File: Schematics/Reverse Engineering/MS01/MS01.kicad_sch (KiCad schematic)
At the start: 69 parts, among them Q1 S1007, Q10 PNP, Q11 PNP, Q12 PNP, Q2 2N1304, Q3 PNP, Q4 2N1304, Q5 2N1304, Q6 PNP, Q7 PNP, Q8 PNP, Q9 PNP, U1 RLIC-12D

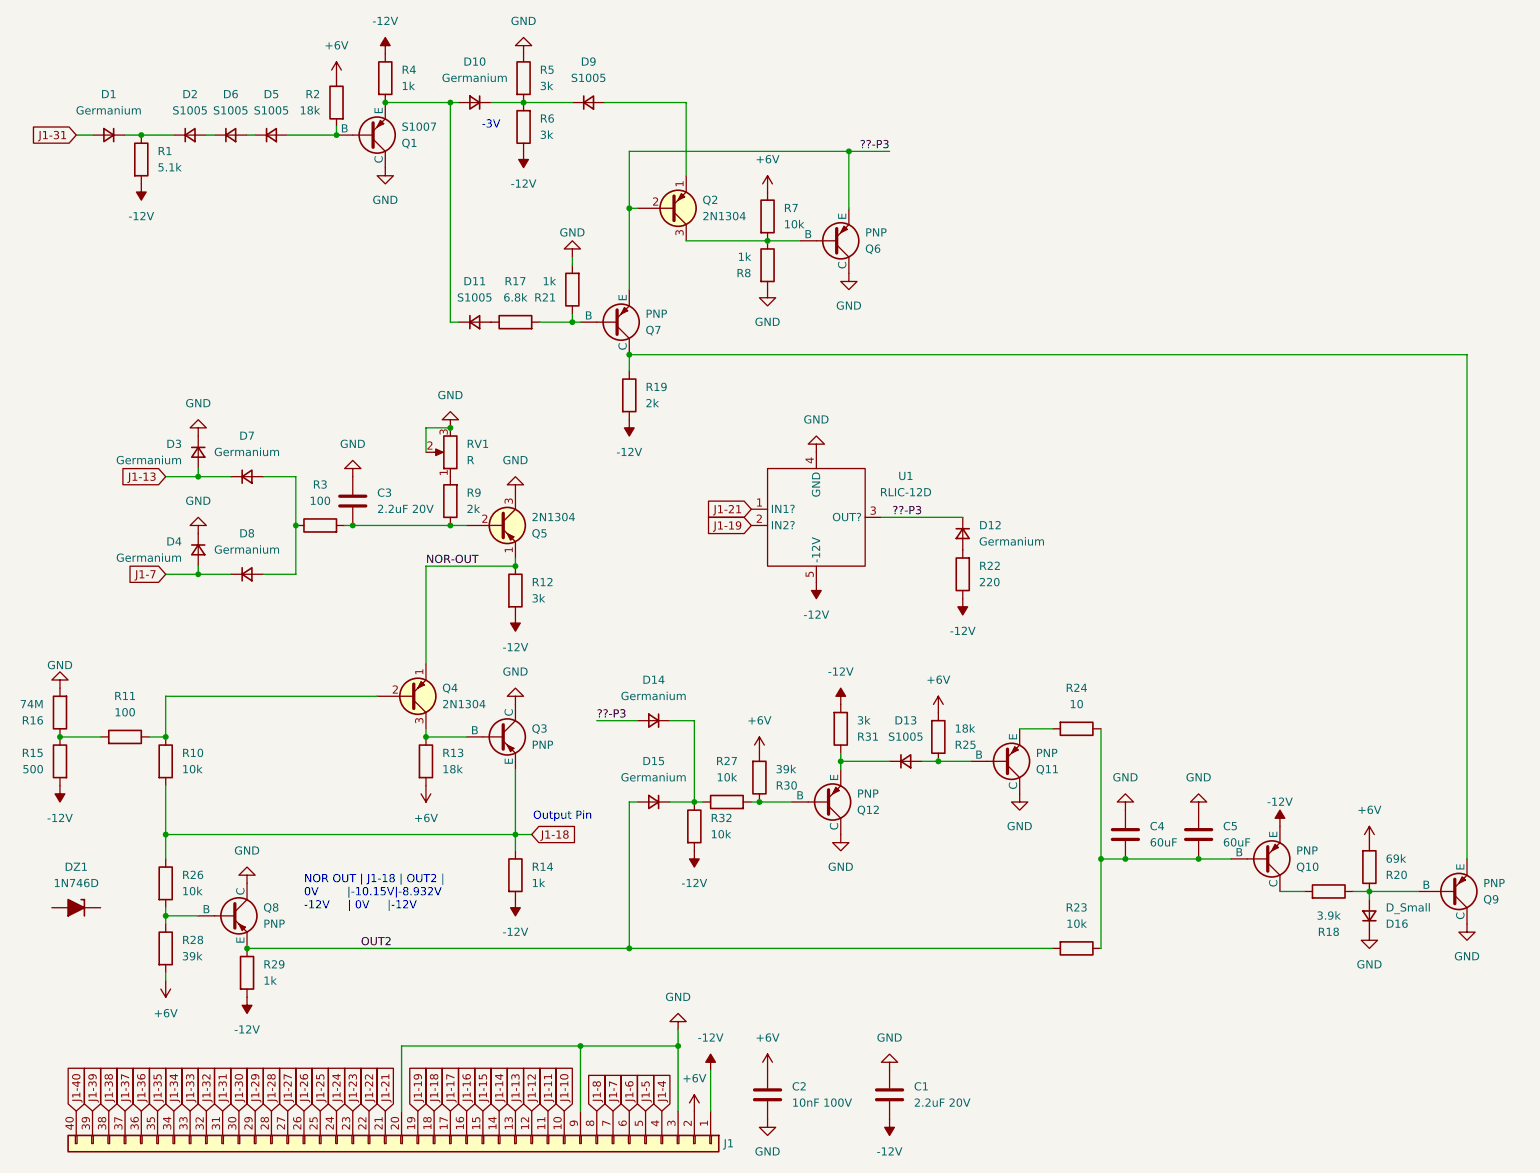
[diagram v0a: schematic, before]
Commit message: MS01 Reverse Engineering
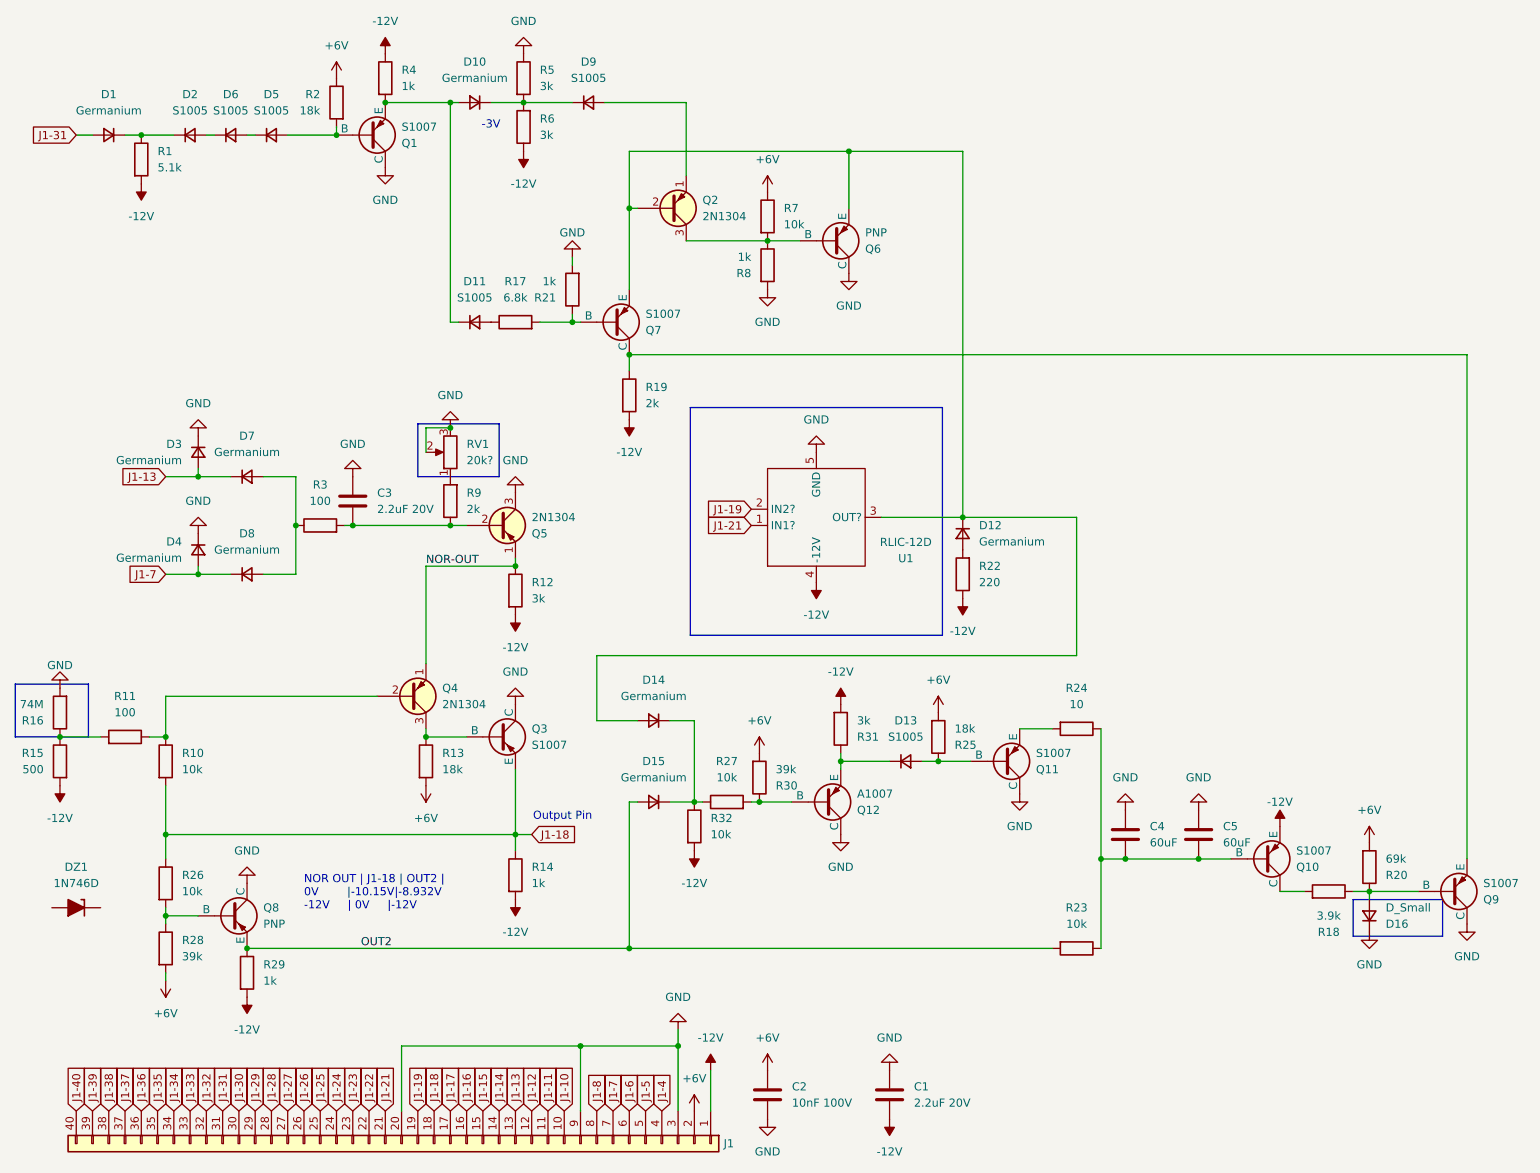
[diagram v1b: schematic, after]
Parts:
- Q10, Q11, Q3, Q7, Q9: value PNP -> S1007
- Q12: value PNP -> A1007
- RV1: value R -> 20k?
- U1: footprint (none) -> MS01:RLIC-12D
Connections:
- net -12V: now also U1.4 (-12V); no longer U1.5 (-12V)
- net GND: now also U1.5 (GND); no longer U1.4 (GND)
- net ??-P3: no longer names the net of D12.1 (K), D14.2 (A), Q2.2 (B), Q6.3 (E), Q7.3 (E), U1.3 (OUT?)
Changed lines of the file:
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@@
 	(generator_version "9.0")
 	(paper "A4")
+	(rectangle
+		(start 13.335 118.745)
+		(end 24.765 127)
+		(stroke
+			(width 0)
+			(type default)
+		)
+		(fill
+			(type none)
+		)
+	)
+	(rectangle
+		(start 76.2 78.105)
+		(end 88.9 86.36)
+		(stroke
+			(width 0)
+			(type default)
+		)
+		(fill
+			(type none)
+		)
+	)
+	(rectangle
+		(start 118.745 75.565)
+		(end 158.115 111.125)
+		(stroke
+			(width 0)
+			(type default)
+		)
+		(fill
+			(type none)
+		)
+	)
+	(rectangle
+		(start 222.25 152.4)
+		(end 236.22 158.115)
+		(stroke
+			(width 0)
+			(type default)
+		)
+		(fill
+			(type none)
+		)
+	)
 	(text "-3V"
 		(exclude_from_sim no)
@@
 	)
 	(junction
+		(at 161.29 92.71)
+		(diameter 0)
+		(color 0 0 0 0)
+	)
+	(junction
 		(at 116.84 175.26)
 		(diameter 0)
@@
 	(wire
 		(pts
+			(xy 104.14 114.3) (xy 179.07 114.3)
+		)
+		(stroke
+			(width 0)
+			(type default)
+		)
+	)
+	(wire
+		(pts
 			(xy 119.38 124.46) (xy 119.38 137.16)
 		)
@@
 	(wire
 		(pts
+			(xy 179.07 92.71) (xy 161.29 92.71)
+		)
+		(stroke
+			(width 0)
+			(type default)
+		)
+	)
+	(wire
+		(pts
 			(xy 41.91 85.09) (xy 41.91 86.36)
 		)
@@
 	(wire
 		(pts
-			(xy 149.86 35.56) (xy 143.51 35.56)
+			(xy 143.51 35.56) (xy 161.29 35.56)
 		)
 		(stroke
@@
 	(wire
 		(pts
+			(xy 161.29 92.71) (xy 161.29 35.56)
+		)
+		(stroke
+			(width 0)
+			(type default)
+		)
+	)
+	(wire
+		(pts
 			(xy 92.71 27.94) (xy 87.63 27.94)
 		)
@@
 	(wire
 		(pts
+			(xy 179.07 114.3) (xy 179.07 92.71)
+		)
+		(stroke
+			(width 0)
+			(type default)
+		)
+	)
+	(wire
+		(pts
 			(xy 77.47 100.33) (xy 77.47 115.57)
 		)
@@
 	(wire
 		(pts
+			(xy 104.14 124.46) (xy 104.14 114.3)
+		)
+		(stroke
+			(width 0)
+			(type default)
+		)
+	)
+	(wire
+		(pts
 			(xy 109.22 67.31) (xy 240.03 67.31)
 		)
@@
 		)
 	)
-	(label "??-P3"
-		(at 149.86 35.56 180)
-		(effects
-			(font
-				(size 1.27 1.27)
-			)
-			(justify right bottom)
-		)
-	)
-	(label "??-P3"
-		(at 154.94 92.71 180)
-		(effects
-			(font
-				(size 1.27 1.27)
-			)
-			(justify right bottom)
-		)
-	)
-	(label "??-P3"
-		(at 104.14 124.46 0)
-		(effects
-			(font
-				(size 1.27 1.27)
-			)
-			(justify left bottom)
-		)
-	)
 	(label "OUT2"
 		(at 67.31 160.02 0)
@@
 	(global_label "J1-19"
 		(shape input)
-		(at 128.27 93.98 180)
+		(at 128.27 91.44 180)
 		(fields_autoplaced yes)
 		(effects
@@
 		)
 		(property "Intersheetrefs" "${INTERSHEET_REFS}"
-			(at 119.1163 93.98 0)
+			(at 119.1163 91.44 0)
 			(effects
 				(font
@@
 	(global_label "J1-21"
 		(shape input)
-		(at 128.27 91.44 180)
+		(at 128.27 93.98 180)
 		(fields_autoplaced yes)
 		(effects
@@
 		)
 		(property "Intersheetrefs" "${INTERSHEET_REFS}"
-			(at 119.1163 91.44 0)
+			(at 119.1163 93.98 0)
 			(effects
 				(font
@@
 			)
 		)
-		(property "Value" "PNP"
+		(property "Value" "S1007"
 			(at 172.72 129.5401 0)
 			(effects
@@
 			)
 		)
-		(property "Value" "R"
+		(property "Value" "20k?"
 			(at 83.82 83.8199 0)
 			(effects
@@
 			)
 		)
-		(property "Value" "PNP"
+		(property "Value" "S1007"
 			(at 213.36 144.7801 0)
 			(effects
@@
 	(symbol
 		(lib_id "power:-12V")
-		(at 138.43 102.87 180)
+		(at 138.43 102.87 0)
+		(mirror x)
 		(unit 1)
 		(exclude_from_sim no)
@@
 			)
 		)
-		(property "Value" "PNP"
+		(property "Value" "S1007"
 			(at 242.57 149.8601 0)
 			(effects
@@
 			)
 		)
-		(property "Value" "PNP"
+		(property "Value" "S1007"
 			(at 111.76 60.9601 0)
 			(effects
@@
 		(lib_id "MS01:RLIC-12D")
 		(at 138.43 92.71 0)
+		(mirror x)
 		(unit 1)
 		(exclude_from_sim no)
@@
 		(fields_autoplaced yes)
 		(property "Reference" "U1"
-			(at 152.4 86.2898 0)
+			(at 152.4 99.1302 0)
 			(effects
 				(font
@@
 		)
 		(property "Value" "RLIC-12D"
-			(at 152.4 88.8298 0)
+			(at 152.4 96.5902 0)
 			(effects
 				(font
@@
 			)
 		)
-		(property "Footprint" ""
+		(property "Footprint" "MS01:RLIC-12D"
 			(at 138.43 92.71 0)
 			(effects
@@
 	(symbol
 		(lib_id "power:GND")
-		(at 138.43 82.55 180)
+		(at 138.43 82.55 0)
+		(mirror x)
 		(unit 1)
 		(exclude_from_sim no)
@@
 			)
 		)
-		(property "Value" "PNP"
+		(property "Value" "S1007"
 			(at 93.98 128.2699 0)
 			(effects
@@
 			)
 		)
-		(property "Value" "PNP"
+		(property "Value" "A1007"
 			(at 144.78 135.8901 0)
 			(effects

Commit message: Finished MS01 PCB and Revised Schematic
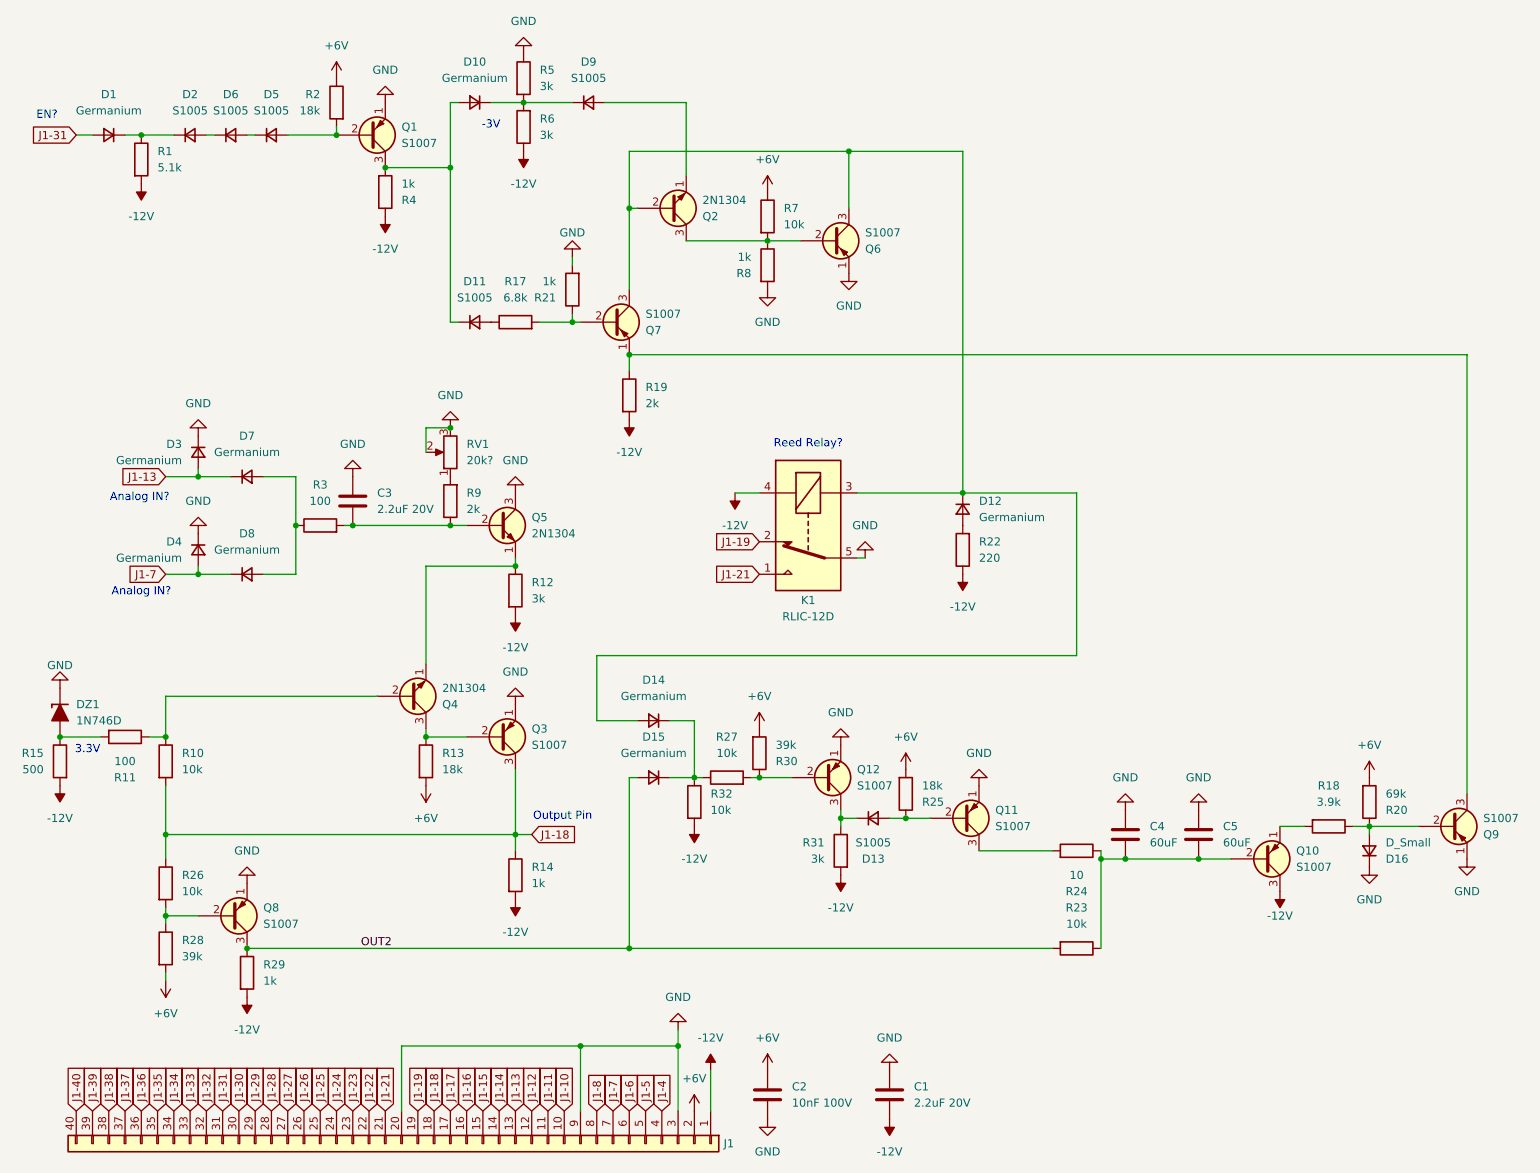
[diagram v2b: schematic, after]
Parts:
- removed Q1: S1007, Package_TO_SOT_THT:TO-5-3, symbol Simulation_SPICE:PNP
- removed Q2, Q4, Q5: 2N1304, Package_TO_SOT_THT:TO-5-3, symbol PCM_Transistor_BJT_AKL:Q_PNP_Generic_EBC
- removed R16: 74M, Resistor_THT:R_Axial_DIN0207_L6.3mm_D2.5mm_P10.16mm_Horizontal, symbol Device:R
- added Q1: S1007, Package_TO_SOT_THT:TO-5-3, symbol PCM_Transistor_BJT_AKL:Q_PNP_Generic_EBC
- added Q2, Q4, Q5: 2N1304, Package_TO_SOT_THT:TO-5-3, symbol PCM_Transistor_BJT_AKL:Q_NPN_Generic_EBC
- DZ1: footprint (none) -> Diode_THT:D_A-405_P12.70mm_Horizontal
- Q10, Q11, Q3, Q7, Q9: symbol Simulation_SPICE:PNP -> PCM_Transistor_BJT_AKL:Q_PNP_Generic_EBC
- Q12: value A1007 -> S1007; symbol Simulation_SPICE:PNP -> PCM_Transistor_BJT_AKL:Q_PNP_Generic_EBC
- Q6, Q8: value PNP -> S1007; symbol Simulation_SPICE:PNP -> PCM_Transistor_BJT_AKL:Q_PNP_Generic_EBC
- renumbered U1 to K1
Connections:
- net GND: now also DZ1.1 (K), Q1.1 (E), Q5.3 (C)
- net at D5.2 (A), R2.2: now also Q1.2 (B)
- net at D10.2 (A), D11.1 (K), R4.2: now also Q1.3 (C)
- net at R10.1, R11.1: now also Q4.2 (B)
- net at R11.2, R15.1: now also DZ1.2 (A)
- net at Q6.2 (B), R7.2, R8.1: now also Q2.3 (C)
- net at D12.1 (K), D14.2 (A), K1.3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: now also Q2.2 (B)
- net at Q3.2 (B), R13.1: now also Q4.3 (C)
- net at C3.1, R3.2, R9.1: now also Q5.2 (B)
- net at D9.2 (A): now also Q2.1 (E)
- net NOR-OUT: no longer names the net of R12.1
- net NOR-OUT: now also Q4.1 (E), Q5.1 (E)
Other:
- note added: "3.3V"
- note added: "Analog IN?"
- note added: "EN?"
- note added: "Reed Relay?"
- note removed: "NOR OUT | J1-18 | OUT2 | 0V |-10.15V|-8.932V -12V | 0V |-12V"
- moved on the sheet: D12, D13, D15, D16, DZ1, Q11, Q12, Q9, R18, R20, R22, R24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

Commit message: Fixed Missing Zener in DM23 and Added MS01 pdf
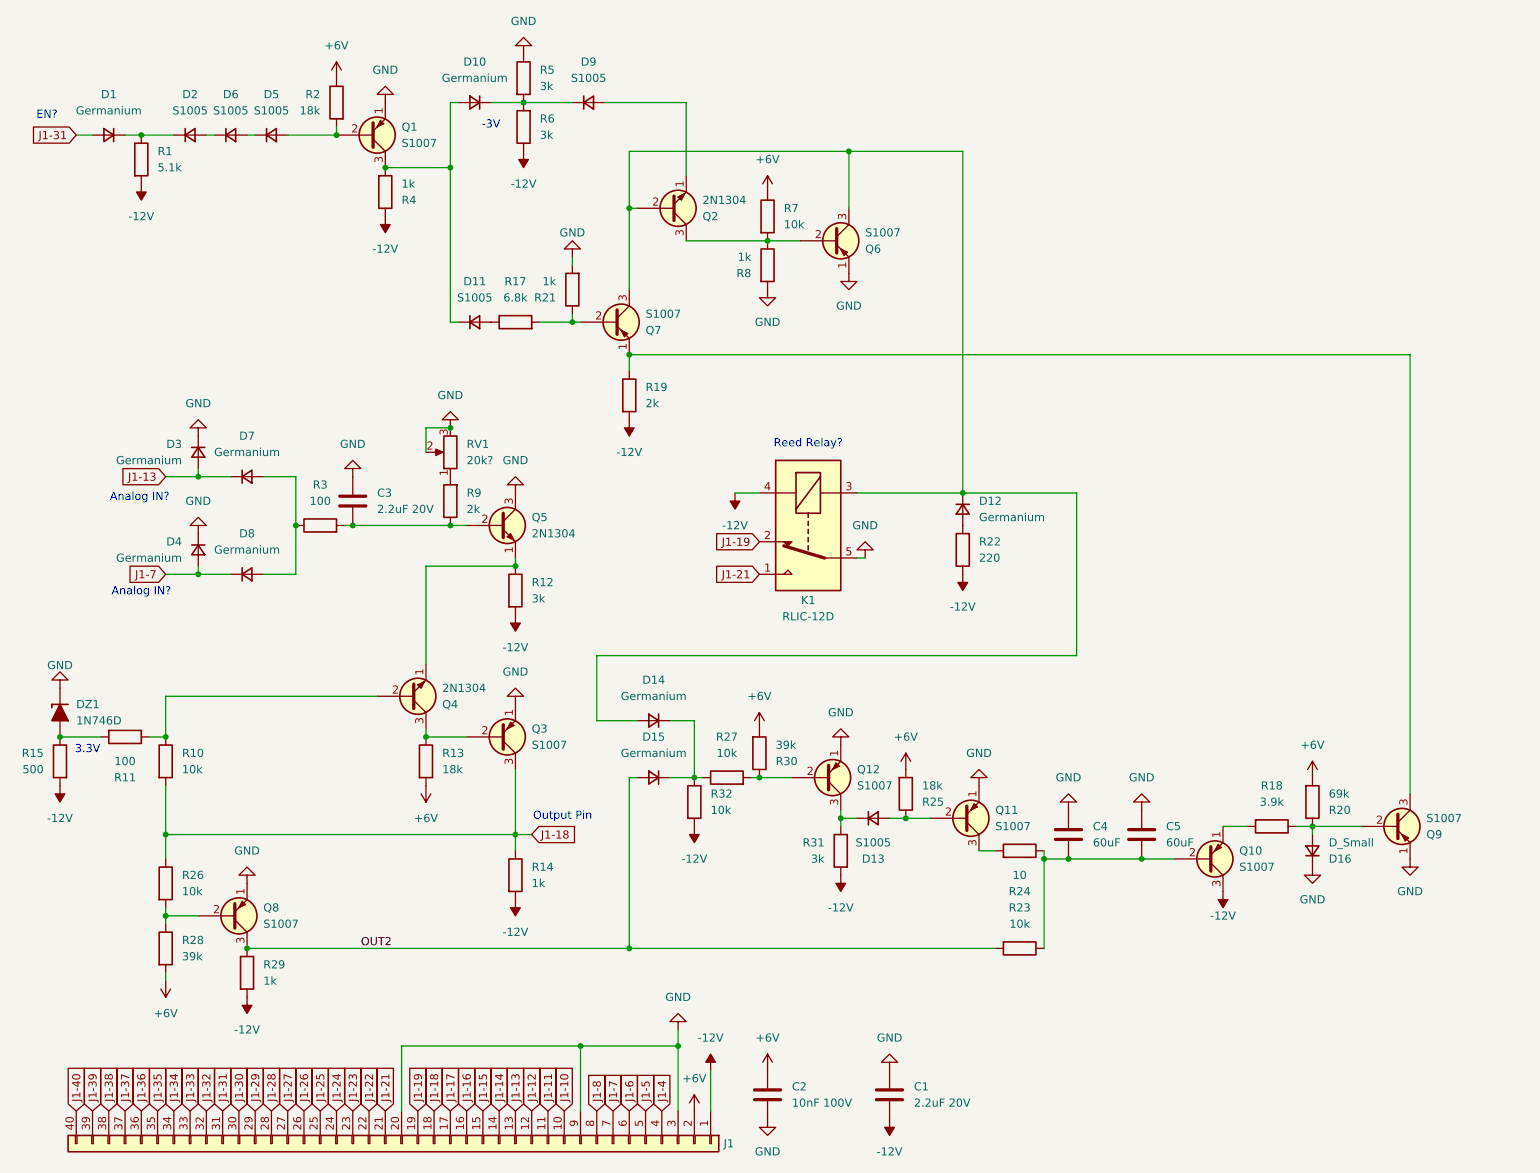
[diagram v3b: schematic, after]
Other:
- moved on the sheet: C4, C5, D16, Q10, Q9, R18, R20, R23, R24
